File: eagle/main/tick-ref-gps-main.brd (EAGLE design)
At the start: 106.7 x 114.3 mm, 39 parts, among them CN1 Power In, CN2 ISP, CN3 Ant. BP, CN4 Ant. GPS, CN5 Serial Program, CN6 Backplane, CN7 Front Panel, U1 ATMEGA168-AU, U2 RAC02-05SC, U3 MAX232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

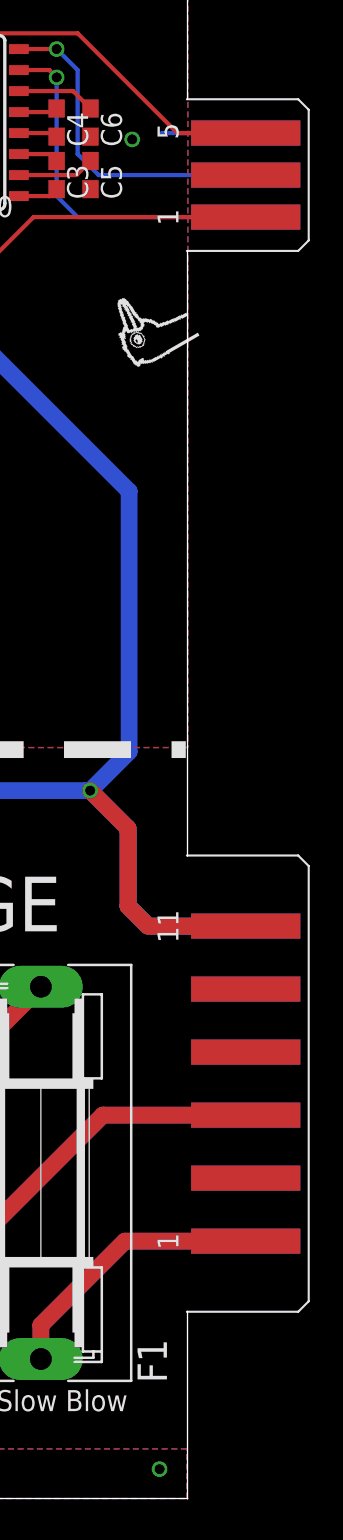
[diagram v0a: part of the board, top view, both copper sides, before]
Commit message: Finished board outline.
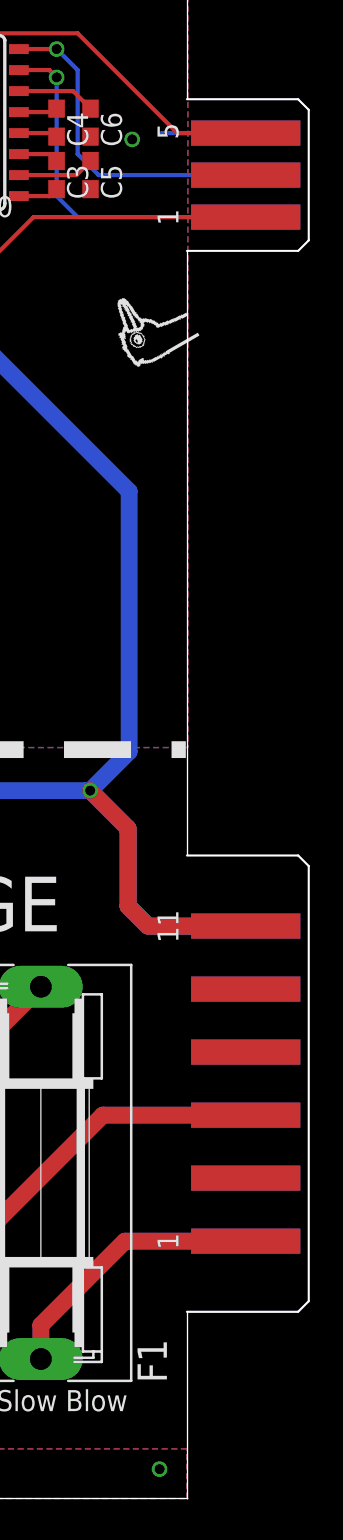
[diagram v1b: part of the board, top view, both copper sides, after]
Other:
- board size 106.7 x 114.3 mm -> 114 x 114.3 mm
